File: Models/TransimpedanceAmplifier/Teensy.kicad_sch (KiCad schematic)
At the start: 1 part, among them U1 Teensy4.1

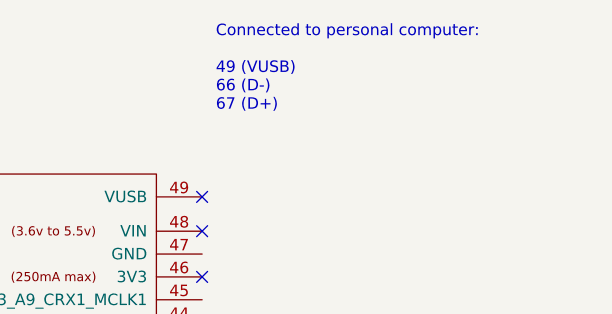
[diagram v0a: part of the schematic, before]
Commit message: Specified the power I/O sheet pins for the ADC
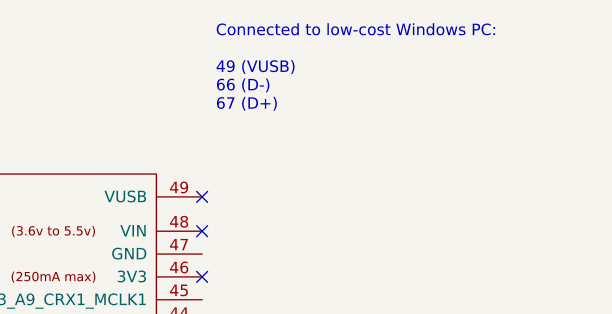
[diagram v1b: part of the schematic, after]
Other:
- note added: "Connected to low-cost Windows PC: 49 (VUSB) 66 (D-) 67 (D+)"
- note removed: "Connected to personal computer: 49 (VUSB) 66 (D-) 67 (D+)"
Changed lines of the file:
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@@
 	(generator_version "9.0")
 	(paper "A4")
-	(text "Connected to personal computer:\n\n49 (VUSB)\n66 (D-)\n67 (D+)"
+	(text "Connected to low-cost Windows PC:\n\n49 (VUSB)\n66 (D-)\n67 (D+)"
 		(exclude_from_sim no)
 		(at 184.404 39.116 0)

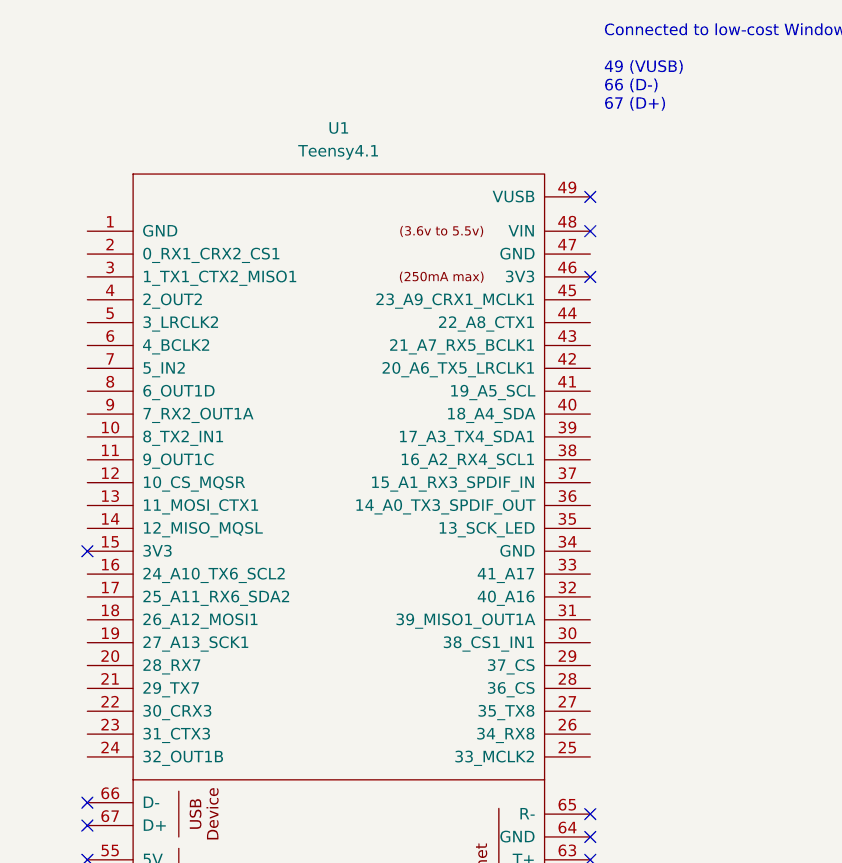
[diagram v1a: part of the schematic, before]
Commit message: Assigned all the SPI pins
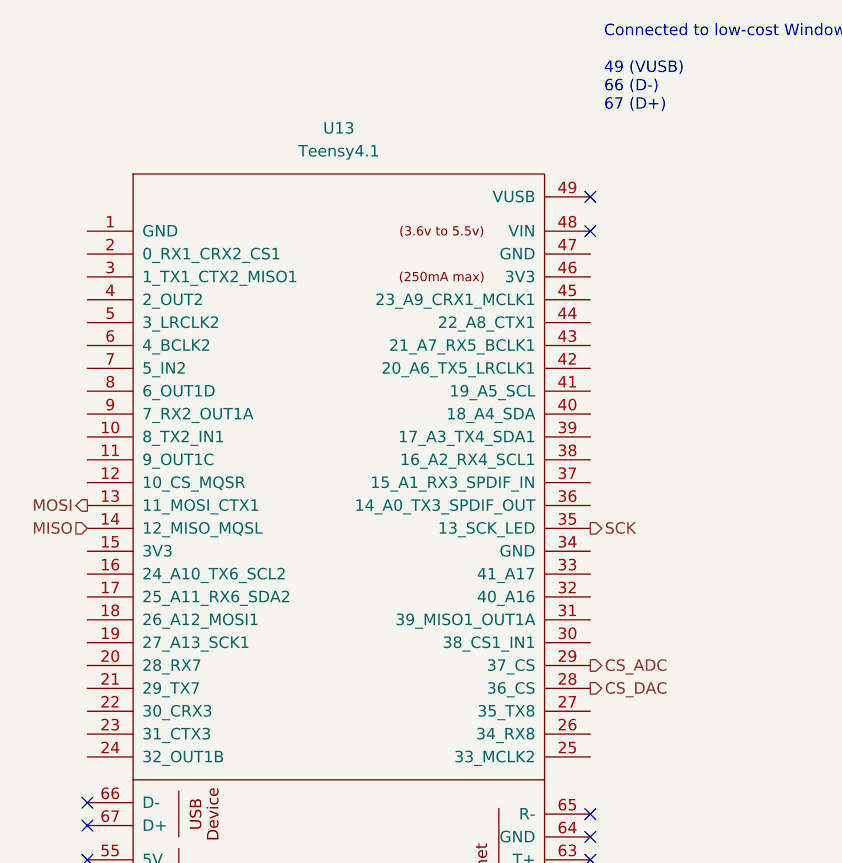
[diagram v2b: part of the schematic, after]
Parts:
- renumbered U1 to U13
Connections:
- net MOSI: now reaches U13.13 (11_MOSI_CTX1)
- net MISO: now reaches U13.14 (12_MISO_MQSL)
- net CS_DAC: now reaches U13.28 (36_CS)
- net CS_ADC: now reaches U13.29 (37_CS)
- net SCK: now reaches U13.35 (13_SCK_LED)
- no-connect marks 22 -> 20
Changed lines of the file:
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@@
-	)
-	(no_connect
-		(at 182.88 62.23)
 	)
 	(no_connect
@@
 	)
 	(no_connect
-		(at 127 92.71)
-	)
-	(no_connect
 		(at 182.88 57.15)
+	)
+	(hierarchical_label "MISO"
+		(shape input)
+		(at 127 90.17 180)
+		(effects
+			(font
+				(size 1.27 1.27)
+			)
+			(justify right)
+		)
+	)
+	(hierarchical_label "MOSI"
+		(shape output)
+		(at 127 87.63 180)
+		(effects
+			(font
+				(size 1.27 1.27)
+			)
+			(justify right)
+		)
+	)
+	(hierarchical_label "CS_ADC"
+		(shape output)
+		(at 182.88 105.41 0)
+		(effects
+			(font
+				(size 1.27 1.27)
+			)
+			(justify left)
+		)
+	)
+	(hierarchical_label "SCK"
+		(shape output)
+		(at 182.88 90.17 0)
+		(effects
+			(font
+				(size 1.27 1.27)
+			)
+			(justify left)
+		)
+	)
+	(hierarchical_label "CS_DAC"
+		(shape output)
+		(at 182.88 107.95 0)
+		(effects
+			(font
+				(size 1.27 1.27)
+			)
+			(justify left)
+		)
 	)
 	(symbol
@@
 		(dnp no)
 		(fields_autoplaced yes)
-		(property "Reference" "U1"
+		(property "Reference" "U13"
 			(at 154.94 45.72 0)
 			(effects
@@
 		(instances
 			(project "TransimpedanceAmplifier"
-				(path "/ec9f2ae3-e40d-40eb-9760-2b611ee8efd1/dc20c4fb-dcde-4b02-ae84-952f4ab38fe2"
-					(reference "U1")
+				(path "/ec9f2ae3-e40d-40eb-9760-2b611ee8efd1/7e303428-a18c-4ad4-b002-5ab9c6631588/801eb825-6f09-44eb-9a12-14faa51f83f1"
+					(reference "U13")
 					(unit 1)
 				)

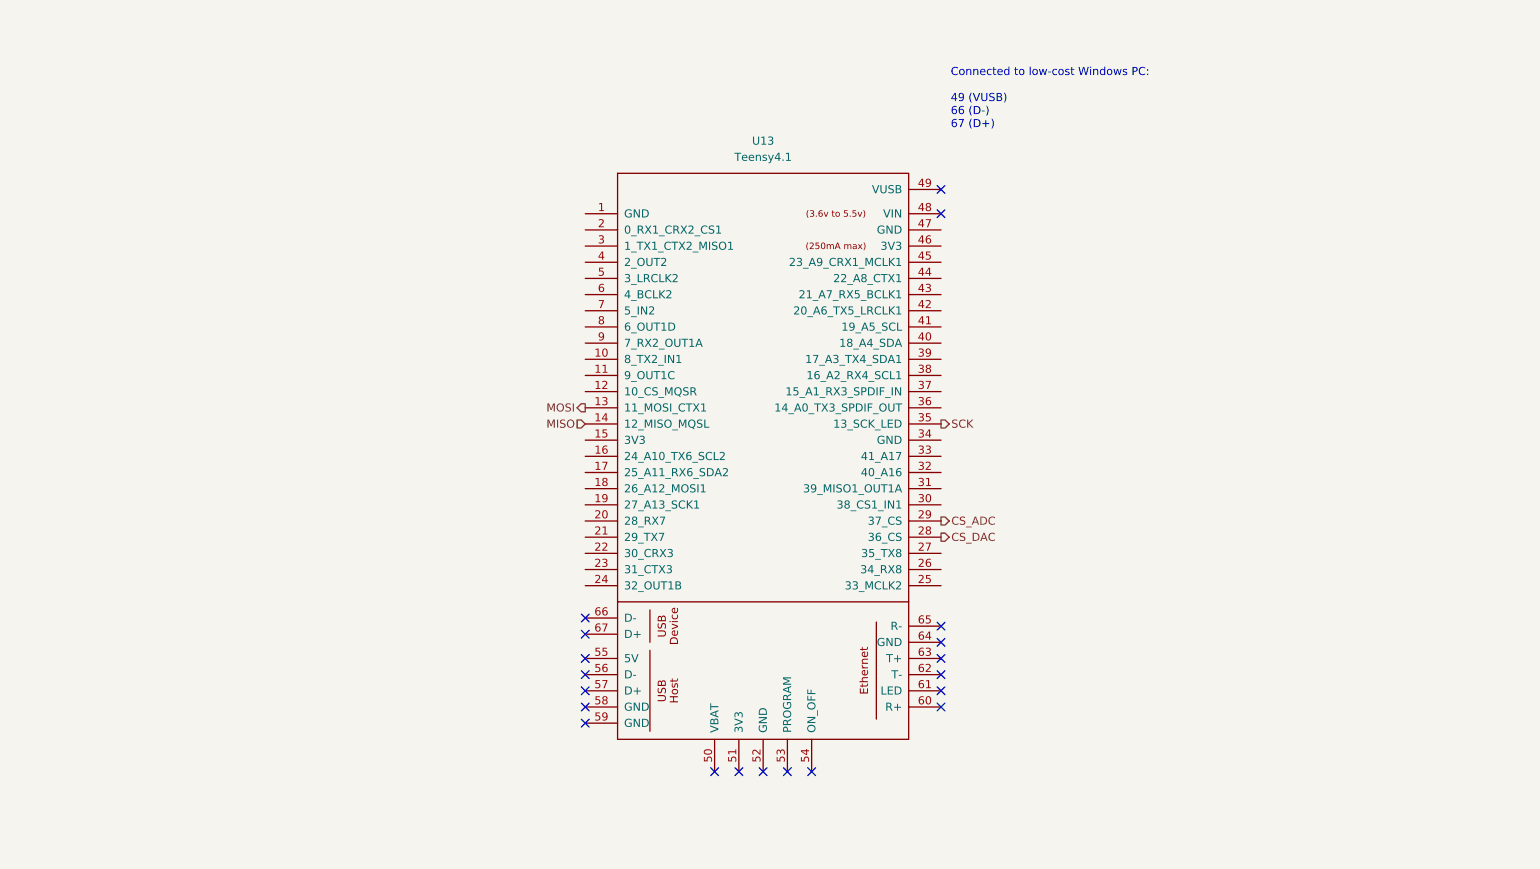
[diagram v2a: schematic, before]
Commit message: This should be all of the pin headers
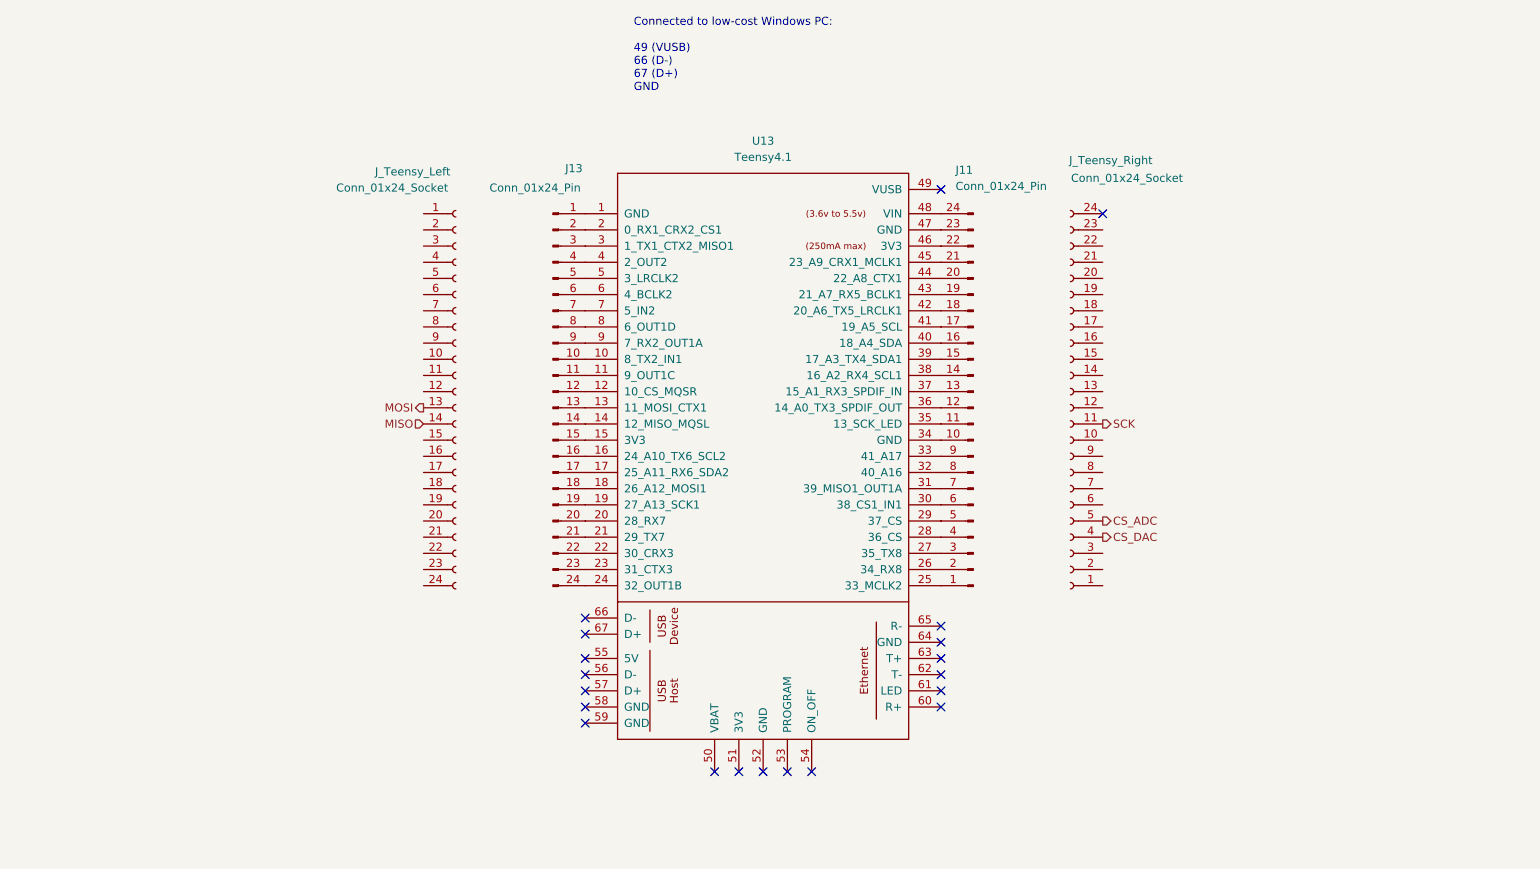
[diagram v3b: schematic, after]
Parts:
- added J11, J13: Conn_01x24_Pin, symbol Connector:Conn_01x24_Pin
- added J_Teensy_Left, J_Teensy_Right: Conn_01x24_Socket, symbol Connector:Conn_01x24_Socket
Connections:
- net CS_ADC: now also J_Teensy_Right.5 (Pin_5); no longer U13.29 (37_CS)
- net CS_DAC: now also J_Teensy_Right.4 (Pin_4); no longer U13.28 (36_CS)
- net MISO: now also J_Teensy_Left.14 (Pin_14); no longer U13.14 (12_MISO_MQSL)
- net MOSI: now also J_Teensy_Left.13 (Pin_13); no longer U13.13 (11_MOSI_CTX1)
- net SCK: now also J_Teensy_Right.11 (Pin_11); no longer U13.35 (13_SCK_LED)
- net at U13.1 (GND): now also J13.1 (Pin_1)
- net at U13.10 (8_TX2_IN1): now also J13.10 (Pin_10)
- net at U13.11 (9_OUT1C): now also J13.11 (Pin_11)
- net at U13.12 (10_CS_MQSR): now also J13.12 (Pin_12)
- net at U13.15 (3V3): now also J13.15 (Pin_15)
- net at U13.16 (24_A10_TX6_SCL2): now also J13.16 (Pin_16)
- net at U13.17 (25_A11_RX6_SDA2): now also J13.17 (Pin_17)
- net at U13.18 (26_A12_MOSI1): now also J13.18 (Pin_18)
- net at U13.19 (27_A13_SCK1): now also J13.19 (Pin_19)
- net at U13.2 (0_RX1_CRX2_CS1): now also J13.2 (Pin_2)
- net at U13.20 (28_RX7): now also J13.20 (Pin_20)
- net at U13.21 (29_TX7): now also J13.21 (Pin_21)
- net at U13.22 (30_CRX3): now also J13.22 (Pin_22)
- net at U13.23 (31_CTX3): now also J13.23 (Pin_23)
- net at U13.24 (32_OUT1B): now also J13.24 (Pin_24)
- net at U13.25 (33_MCLK2): now also J11.1 (Pin_1)
- net at U13.26 (34_RX8): now also J11.2 (Pin_2)
- net at U13.27 (35_TX8): now also J11.3 (Pin_3)
- net at U13.3 (1_TX1_CTX2_MISO1): now also J13.3 (Pin_3)
- net at U13.30 (38_CS1_IN1): now also J11.6 (Pin_6)
- net at U13.31 (39_MISO1_OUT1A): now also J11.7 (Pin_7)
- net at U13.32 (40_A16): now also J11.8 (Pin_8)
- net at U13.33 (41_A17): now also J11.9 (Pin_9)
- net at U13.34 (GND): now also J11.10 (Pin_10)
- net at U13.36 (14_A0_TX3_SPDIF_OUT): now also J11.12 (Pin_12)
- net at U13.37 (15_A1_RX3_SPDIF_IN): now also J11.13 (Pin_13)
- net at U13.38 (16_A2_RX4_SCL1): now also J11.14 (Pin_14)
- net at U13.39 (17_A3_TX4_SDA1): now also J11.15 (Pin_15)
- net at U13.4 (2_OUT2): now also J13.4 (Pin_4)
- net at U13.40 (18_A4_SDA): now also J11.16 (Pin_16)
- net at U13.41 (19_A5_SCL): now also J11.17 (Pin_17)
- net at U13.42 (20_A6_TX5_LRCLK1): now also J11.18 (Pin_18)
- net at U13.43 (21_A7_RX5_BCLK1): now also J11.19 (Pin_19)
- net at U13.44 (22_A8_CTX1): now also J11.20 (Pin_20)
- net at U13.45 (23_A9_CRX1_MCLK1): now also J11.21 (Pin_21)
- net at U13.46 (3V3): now also J11.22 (Pin_22)
- net at U13.47 (GND): now also J11.23 (Pin_23)
- net at U13.48 (VIN): now also J11.24 (Pin_24)
- net at U13.5 (3_LRCLK2): now also J13.5 (Pin_5)
- net at U13.6 (4_BCLK2): now also J13.6 (Pin_6)
- net at U13.7 (5_IN2): now also J13.7 (Pin_7)
- net at U13.8 (6_OUT1D): now also J13.8 (Pin_8)
- net at U13.9 (7_RX2_OUT1A): now also J13.9 (Pin_9)
- new net: J13.13 (Pin_13), U13.13 (11_MOSI_CTX1)
- new net: J13.14 (Pin_14), U13.14 (12_MISO_MQSL)
- new net: J11.11 (Pin_11), U13.35 (13_SCK_LED)
- new net: J11.4 (Pin_4), U13.28 (36_CS)
- new net: J11.5 (Pin_5), U13.29 (37_CS)
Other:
- note added: "Connected to low-cost Windows PC: 49 (VUSB) 66 (D-) 67 (D+) GND"
- note removed: "Connected to low-cost Windows PC: 49 (VUSB) 66 (D-) 67 (D+)"

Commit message: Save progress
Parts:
- J11, J13, J_Teensy_Left, J_Teensy_Right: Purchase Link (none) -> https://www.digikey.com/en/products/detail/sullins-connecto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
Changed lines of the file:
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@@
+			)
+		)
+		(property "Purchase Link" "https://www.digikey.com/en/products/detail/sullins-connector-solutions/PPPC241LFBN-RC/810196"
+			(at 203.2 87.63 0)
+			(effects
+				(font
+					(size 1.27 1.27)
+				)
+				(hide yes)
 			)
 		)
@@
 			)
 		)
+		(property "Purchase Link" "https://www.digikey.com/en/products/detail/sullins-connector-solutions/PPPC241LFBN-RC/810196"
+			(at 106.68 85.09 0)
+			(effects
+				(font
+					(size 1.27 1.27)
+				)
+				(hide yes)
+			)
+		)
 		(pin "2"
 		)
@@
 			)
 		)
+		(property "Purchase Link" "https://www.digikey.com/en/products/detail/sullins-connector-solutions/PRPC024SAAN-RC/2775230"
+			(at 121.92 85.09 0)
+			(effects
+				(font
+					(size 1.27 1.27)
+				)
+				(hide yes)
+			)
+		)
 		(pin "2"
 		)
@@
 			(at 187.96 87.63 0)
 			(effects
+				(font
+					(size 1.27 1.27)
+				)
+				(hide yes)
+			)
+		)
+		(property "Purchase Link" "https://www.digikey.com/en/products/detail/sullins-connector-solutions/PRPC024SAAN-RC/2775230"
+			(at 187.96 87.63 0)
+			(effects
